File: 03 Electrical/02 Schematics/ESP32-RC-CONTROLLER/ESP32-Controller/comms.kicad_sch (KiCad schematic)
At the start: 0 parts

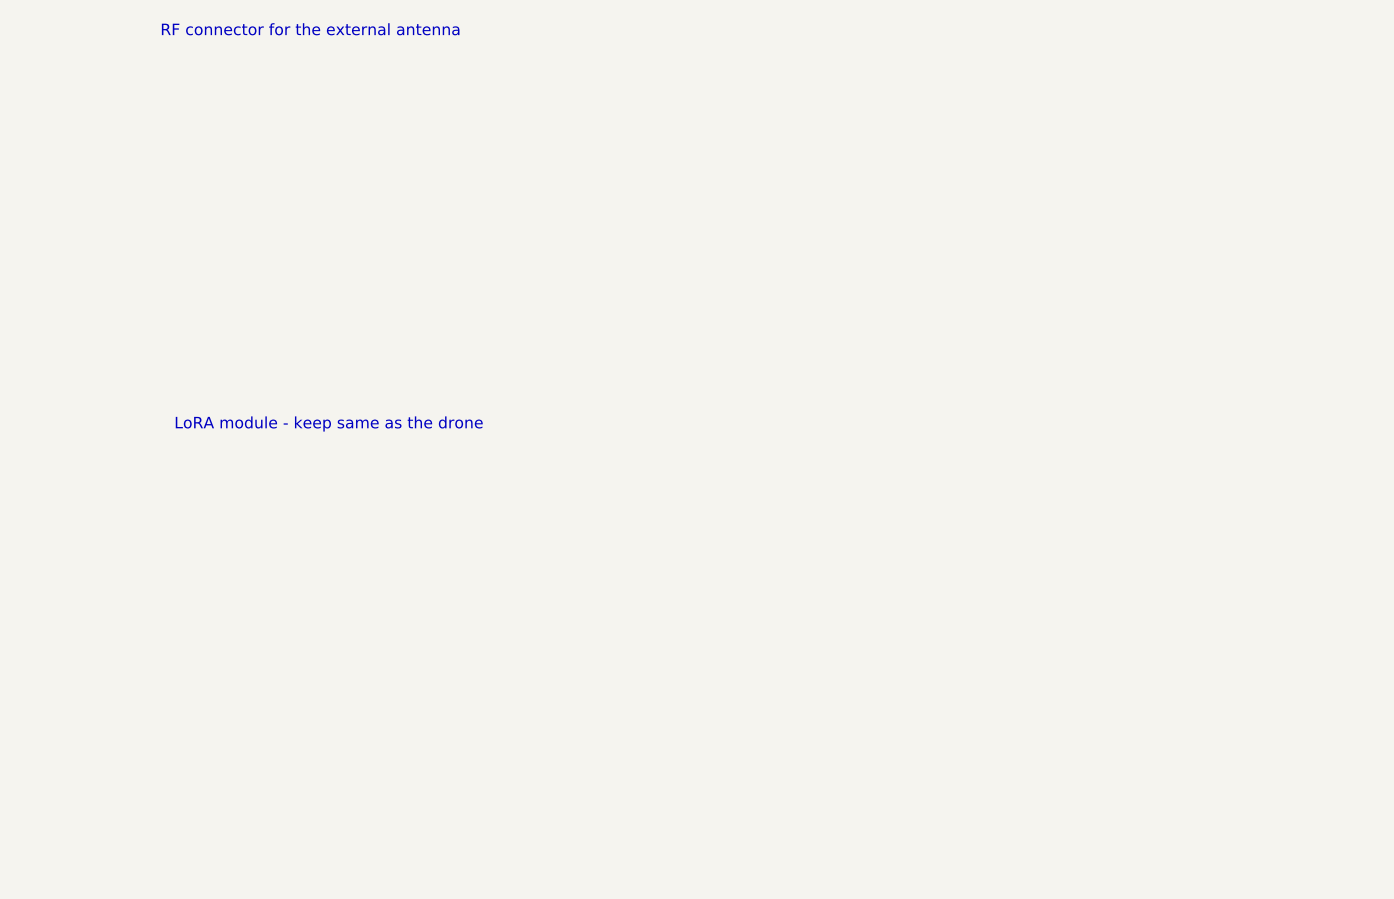
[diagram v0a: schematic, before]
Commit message: added new micro
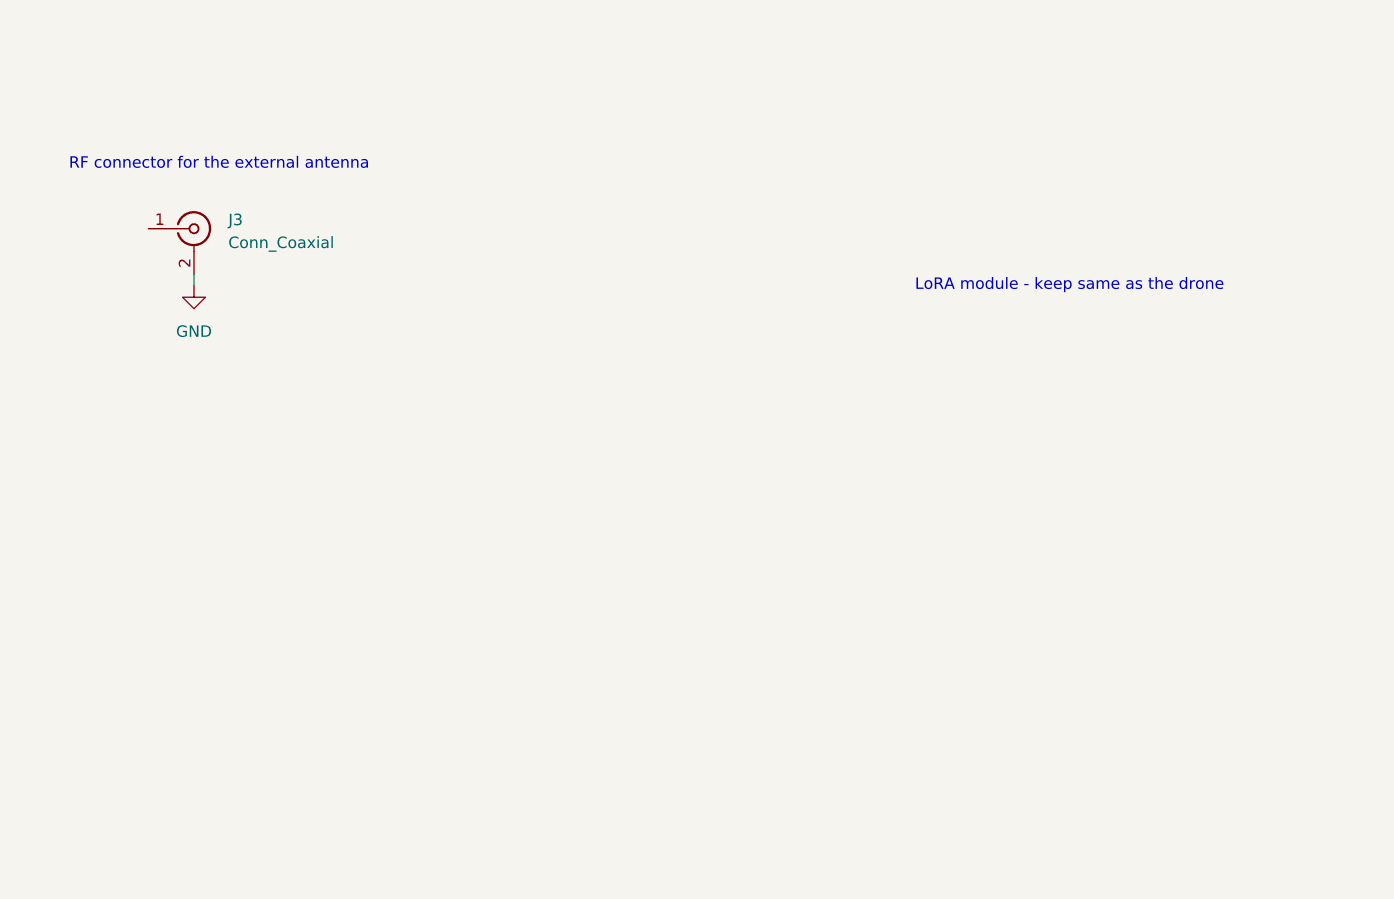
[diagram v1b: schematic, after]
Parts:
- added J3: Conn_Coaxial, symbol Connector:Conn_Coaxial
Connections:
- new net GND: J3.2 (Ext)
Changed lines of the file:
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@@
 	(text "RF connector for the external antenna\n"
 		(exclude_from_sim no)
-		(at 45.974 26.416 0)
+		(at 35.814 41.148 0)
 		(effects
 			(font
@@
 	(text "LoRA module - keep same as the drone\n"
 		(exclude_from_sim no)
-		(at 48.006 70.104 0)
+		(at 130.302 54.61 0)
 		(effects
 			(font
@@
 			)
 		)
+	)
+	(wire
+		(pts
+			(xy 33.02 53.34) (xy 33.02 54.61)
+		)
+		(stroke
+			(width 0)
+			(type default)
+		)
+	)
+	(symbol
+		(lib_id "Connector:Conn_Coaxial")
+		(at 33.02 48.26 0)
+		(unit 1)
+		(exclude_from_sim no)
+		(in_bom yes)
+		(on_board yes)
+		(dnp no)
+		(fields_autoplaced yes)
+		(property "Reference" "J3"
+			(at 36.83 47.2832 0)
+			(effects
+				(font
+					(size 1.27 1.27)
+				)
+				(justify left)
+			)
+		)
+		(property "Value" "Conn_Coaxial"
+			(at 36.83 49.8232 0)
+			(effects
+				(font
+					(size 1.27 1.27)
+				)
+				(justify left)
+			)
+		)
+		(property "Footprint" ""
+			(at 33.02 48.26 0)
+			(effects
+				(font
+					(size 1.27 1.27)
+				)
+				(hide yes)
+			)
+		)
+		(property "Datasheet" "~"
+			(at 33.02 48.26 0)
+			(effects
+				(font
+					(size 1.27 1.27)
+				)
+				(hide yes)
+			)
+		)
+		(property "Description" "coaxial connector (BNC, SMA, SMB, SMC, Cinch/RCA, LEMO, ...)"
+			(at 33.02 48.26 0)
+			(effects
+				(font
+					(size 1.27 1.27)
+				)
+				(hide yes)
+			)
+		)
+		(pin "2"
+		)
+		(pin "1"
+		)
+		(instances
+			(project ""
+				(path "/72483840-4eac-4adb-9948-eab3eb110bd4/8b3b8e05-ba6d-4cbb-9669-d7319321dc44"
+					(reference "J3")
+					(unit 1)
+				)
+			)
+		)
+	)
+	(symbol
+		(lib_id "power:GND")
+		(at 33.02 54.61 0)
+		(unit 1)
+		(exclude_from_sim no)
+		(in_bom yes)
+		(on_board yes)
+		(dnp no)
+		(fields_autoplaced yes)
+		(property "Reference" "#PWR015"
+			(at 33.02 60.96 0)
+			(effects
+				(font
+					(size 1.27 1.27)
+				)
+				(hide yes)
+			)
+		)
+		(property "Value" "GND"
+			(at 33.02 59.69 0)
+			(effects
+				(font
+					(size 1.27 1.27)
+				)
+			)
+		)
+		(property "Footprint" ""
+			(at 33.02 54.61 0)
+			(effects
+				(font
+					(size 1.27 1.27)
+				)
+				(hide yes)
+			)
+		)
+		(property "Datasheet" ""
+			(at 33.02 54.61 0)
+			(effects
+				(font
+					(size 1.27 1.27)
+				)
+				(hide yes)
+			)
+		)
+		(property "Description" "Power symbol creates a global label with name \"GND\" , ground"
+			(at 33.02 54.61 0)
+			(effects
+				(font
+					(size 1.27 1.27)
+				)
+				(hide yes)
+			)
+		)
+		(pin "1"
+		)
+		(instances
+			(project ""
+				(path "/72483840-4eac-4adb-9948-eab3eb110bd4/8b3b8e05-ba6d-4cbb-9669-d7319321dc44"
+					(reference "#PWR015")
+					(unit 1)
+				)
+			)
+		)

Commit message: not sure what changes made
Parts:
- added U5: SX1276, Package_DFN_QFN:QFN-28-1EP_6x6mm_P0.65mm_EP4.8x4.8mm, symbol RF:SX1276
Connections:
- net GND: now also U5.15 (GND), U5.23 (GND), U5.26 (GND), U5.29 (GND)
- new net +3V3: U5.14 (VBAT_DIG), U5.24 (VBAT_RF), U5.3 (VBAT_ANA)
- new net RxTimeout: U5.9 (DIO1)
- new net SPI_MISO: U5.17 (MISO)
- new net SPI_MOSI: U5.18 (MOSI)
- new net SPI_SCK: U5.16 (SCK)
- new net SPI_SS: U5.19 (NSS)
- new net TXDone: U5.8 (DIO0)
- new net ValidHeader: U5.11 (DIO3)
- no-connect marks 0 -> 3
